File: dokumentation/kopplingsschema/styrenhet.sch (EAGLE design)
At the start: 1 part, among them IC1 MEGA16-P

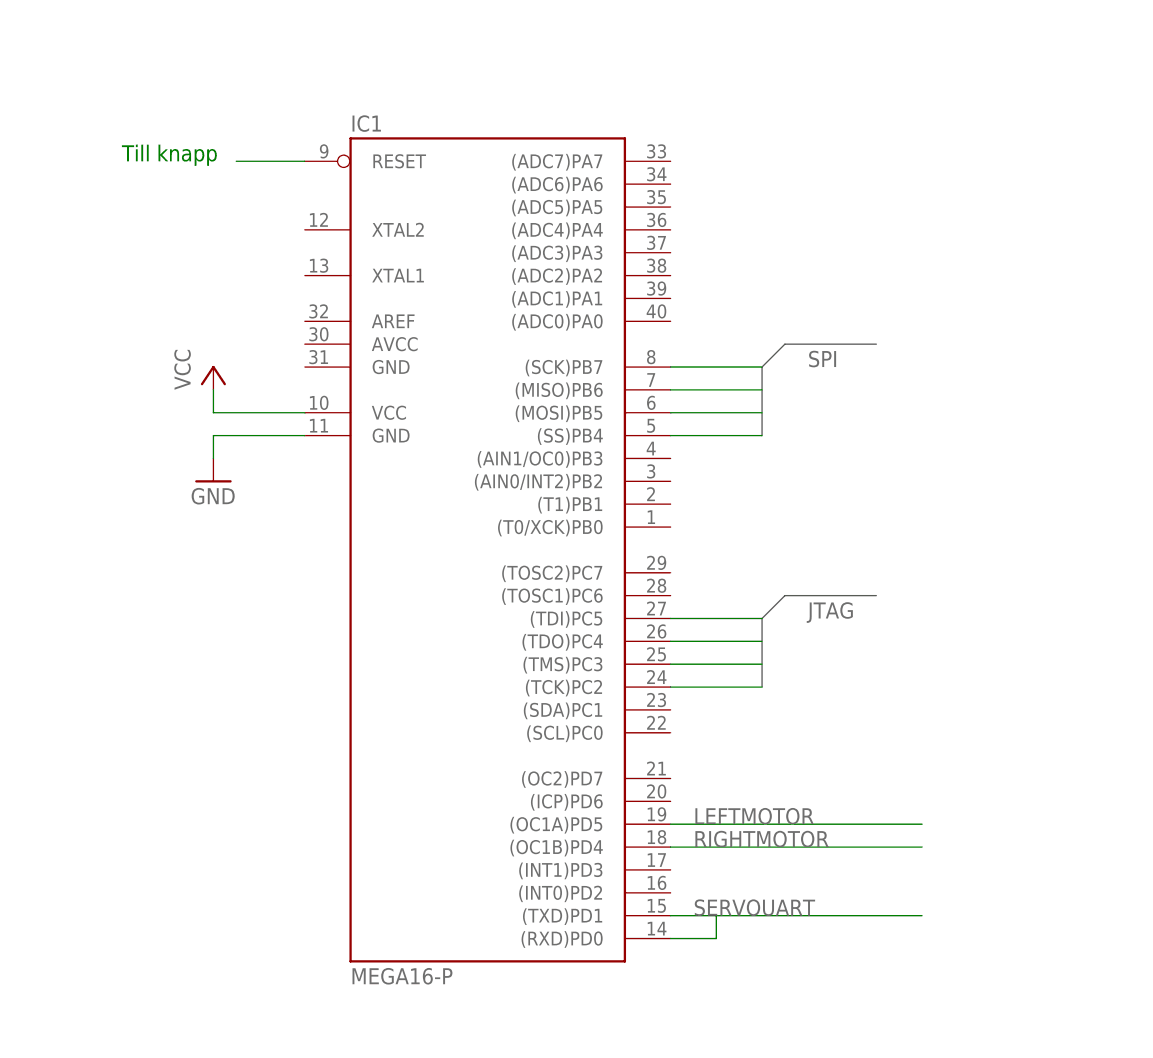
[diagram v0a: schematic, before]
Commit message: Updated circuit diagrams.
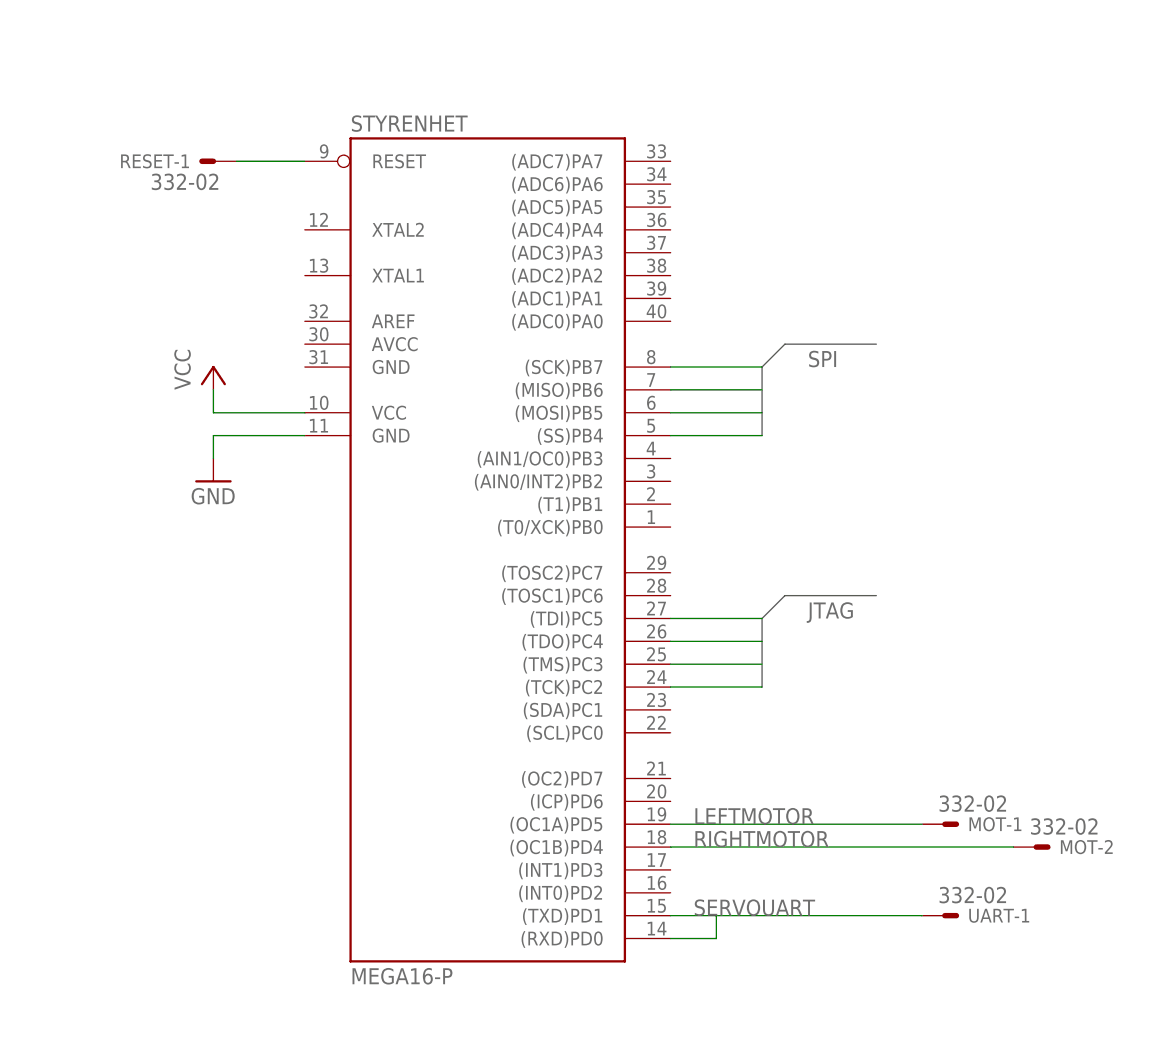
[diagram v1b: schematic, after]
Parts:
- added MOT, RESET, UART: 332-02, con-garry:332-02
- renumbered IC1 to STYRENHET
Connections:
- net LEFTMOTOR: now also MOT-1.S
- net N$1: now also RESET-1.S
- net SERVOUART: now also UART-1.S
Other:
- note removed: "Till knapp"
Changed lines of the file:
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@@
 </classes>
 <parts>
-<part name="IC1" library="atmel" deviceset="MEGA16-P" device=""/>
+<part name="STYRENHET" library="atmel" deviceset="MEGA16-P" device=""/>
 <part name="P+1" library="supply1" deviceset="VCC" device=""/>
 <part name="GND1" library="supply1" deviceset="GND" device=""/>
+<part name="RESET" library="con-garry" deviceset="332-02" device=""/>
+<part name="MOT" library="con-garry" deviceset="332-02" device=""/>
+<part name="UART" library="con-garry" deviceset="332-02" device=""/>
 </parts>
 <sheets>
 <sheet>
 <plain>
-<text x="-25.4" y="88.9" size="1.778" layer="91">Till knapp</text>
 </plain>
 <instances>
-<instance part="IC1" gate="G$1" x="15.24" y="48.26"/>
+<instance part="STYRENHET" gate="G$1" x="15.24" y="48.26"/>
 <instance part="P+1" gate="VCC" x="-15.24" y="66.04"/>
 <instance part="GND1" gate="1" x="-15.24" y="53.34"/>
+<instance part="RESET" gate="-1" x="-15.24" y="88.9" rot="R180"/>
+<instance part="MOT" gate="-1" x="66.04" y="15.24"/>
+<instance part="MOT" gate="-2" x="76.2" y="12.7"/>
+<instance part="UART" gate="-1" x="66.04" y="5.08"/>
 </instances>
 <busses>
@@
 <pinref part="P+1" gate="VCC" pin="VCC"/>
 <wire x1="-15.24" y1="63.5" x2="-15.24" y2="60.96" width="0.1524" layer="91"/>
-<pinref part="IC1" gate="G$1" pin="VCC"/>
+<pinref part="STYRENHET" gate="G$1" pin="VCC"/>
 <wire x1="-15.24" y1="60.96" x2="-5.08" y2="60.96" width="0.1524" layer="91"/>
 </segment>
@@
 <pinref part="GND1" gate="1" pin="GND"/>
 <wire x1="-15.24" y1="55.88" x2="-15.24" y2="58.42" width="0.1524" layer="91"/>
-<pinref part="IC1" gate="G$1" pin="GND"/>
+<pinref part="STYRENHET" gate="G$1" pin="GND"/>
 <wire x1="-15.24" y1="58.42" x2="-5.08" y2="58.42" width="0.1524" layer="91"/>
 </segment>
@@
 <net name="N$1" class="0">
 <segment>
-<pinref part="IC1" gate="G$1" pin="RESET"/>
+<pinref part="STYRENHET" gate="G$1" pin="RESET"/>
 <wire x1="-5.08" y1="88.9" x2="-12.7" y2="88.9" width="0.1524" layer="91"/>
+<pinref part="RESET" gate="-1" pin="S"/>
 </segment>
 </net>
 <net name="N$2" class="0">
 <segment>
-<pinref part="IC1" gate="G$1" pin="(TCK)PC2"/>
+<pinref part="STYRENHET" gate="G$1" pin="(TCK)PC2"/>
 <wire x1="35.56" y1="30.48" x2="45.72" y2="30.48" width="0.1524" layer="91"/>
 </segment>
@@
 <net name="N$3" class="0">
 <segment>
-<pinref part="IC1" gate="G$1" pin="(TMS)PC3"/>
+<pinref part="STYRENHET" gate="G$1" pin="(TMS)PC3"/>
 <wire x1="35.56" y1="33.02" x2="45.72" y2="33.02" width="0.1524" layer="91"/>
 </segment>
@@
 <net name="N$4" class="0">
 <segment>
-<pinref part="IC1" gate="G$1" pin="(TDO)PC4"/>
+<pinref part="STYRENHET" gate="G$1" pin="(TDO)PC4"/>
 <wire x1="35.56" y1="35.56" x2="45.72" y2="35.56" width="0.1524" layer="91"/>
 </segment>
@@
 <net name="N$5" class="0">
 <segment>
-<pinref part="IC1" gate="G$1" pin="(TDI)PC5"/>
+<pinref part="STYRENHET" gate="G$1" pin="(TDI)PC5"/>
 <wire x1="35.56" y1="38.1" x2="45.72" y2="38.1" width="0.1524" layer="91"/>
 </segment>
@@
 <net name="N$6" class="0">
 <segment>
-<pinref part="IC1" gate="G$1" pin="(SS)PB4"/>
+<pinref part="STYRENHET" gate="G$1" pin="(SS)PB4"/>
 <wire x1="35.56" y1="58.42" x2="45.72" y2="58.42" width="0.1524" layer="91"/>
 </segment>
@@
 <net name="N$7" class="0">
 <segment>
-<pinref part="IC1" gate="G$1" pin="(MOSI)PB5"/>
+<pinref part="STYRENHET" gate="G$1" pin="(MOSI)PB5"/>
 <wire x1="35.56" y1="60.96" x2="45.72" y2="60.96" width="0.1524" layer="91"/>
 </segment>
@@
 <net name="N$8" class="0">
 <segment>
-<pinref part="IC1" gate="G$1" pin="(MISO)PB6"/>
+<pinref part="STYRENHET" gate="G$1" pin="(MISO)PB6"/>
 <wire x1="35.56" y1="63.5" x2="45.72" y2="63.5" width="0.1524" layer="91"/>
 </segment>
@@
 <net name="N$9" class="0">
 <segment>
-<pinref part="IC1" gate="G$1" pin="(SCK)PB7"/>
+<pinref part="STYRENHET" gate="G$1" pin="(SCK)PB7"/>
 <wire x1="35.56" y1="66.04" x2="45.72" y2="66.04" width="0.1524" layer="91"/>
 </segment>
@@
 <net name="SERVOUART" class="0">
 <segment>
-<pinref part="IC1" gate="G$1" pin="(TXD)PD1"/>
+<pinref part="STYRENHET" gate="G$1" pin="(TXD)PD1"/>
 <wire x1="35.56" y1="5.08" x2="40.64" y2="5.08" width="0.1524" layer="91"/>
-<pinref part="IC1" gate="G$1" pin="(RXD)PD0"/>
+<pinref part="STYRENHET" gate="G$1" pin="(RXD)PD0"/>
 <wire x1="40.64" y1="5.08" x2="63.5" y2="5.08" width="0.1524" layer="91"/>
 <wire x1="35.56" y1="2.54" x2="40.64" y2="2.54" width="0.1524" layer="91"/>
 <wire x1="40.64" y1="2.54" x2="40.64" y2="5.08" width="0.1524" layer="91"/>
 <label x="38.1" y="5.08" size="1.778" layer="95"/>
+<pinref part="UART" gate="-1" pin="S"/>
 </segment>
 </net>
 <net name="LEFTMOTOR" class="0">
 <segment>
-<pinref part="IC1" gate="G$1" pin="(OC1A)PD5"/>
+<pinref part="STYRENHET" gate="G$1" pin="(OC1A)PD5"/>
 <wire x1="35.56" y1="15.24" x2="63.5" y2="15.24" width="0.1524" layer="91"/>
 <label x="38.1" y="15.24" size="1.778" layer="95"/>
+<pinref part="MOT" gate="-1" pin="S"/>
 </segment>
 </net>
 <net name="RIGHTMOTOR" class="0">
 <segment>
-<pinref part="IC1" gate="G$1" pin="(OC1B)PD4"/>
-<wire x1="35.56" y1="12.7" x2="63.5" y2="12.7" width="0.1524" layer="91"/>
+<pinref part="STYRENHET" gate="G$1" pin="(OC1B)PD4"/>
+<wire x1="35.56" y1="12.7" x2="73.66" y2="12.7" width="0.1524" layer="91"/>
 <label x="38.1" y="12.7" size="1.778" layer="95"/>
 </segment>

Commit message: Updated circuit diagram for prop unit.
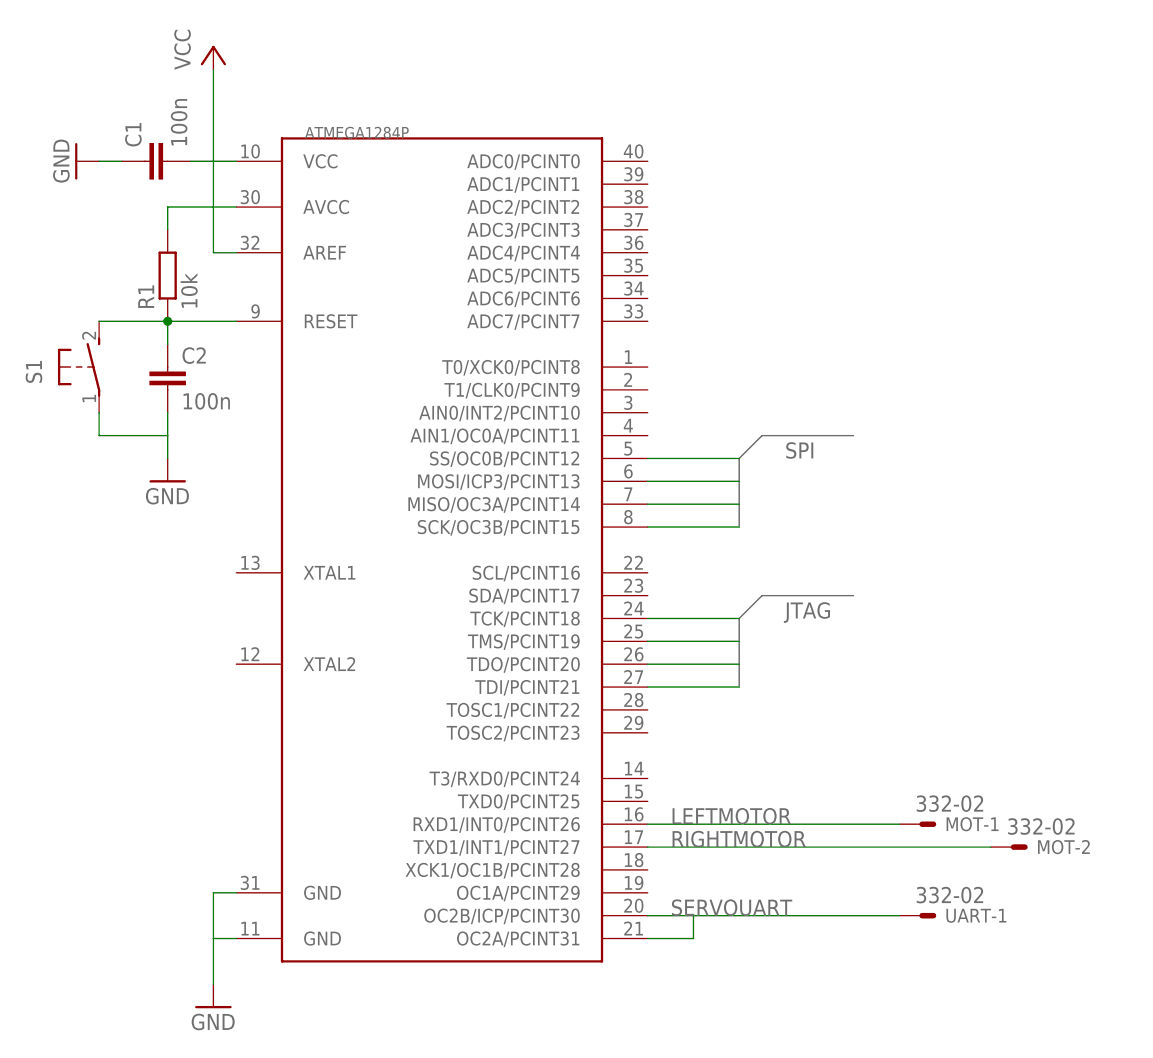
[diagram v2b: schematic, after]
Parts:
- removed RESET: 332-02, con-garry:332-02
- removed STYRENHET: MEGA16-P, atmel:MEGA16-P
- added ATMEGA1284P: (no value), 1284p:MEGA1284P
- added C1, C2: 100n, rcl:C-EU025-050X050
- added R1: 10k, resistor:R-EU_0204/2V
- added S1: (no value), switch-omron:31-XX
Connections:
- removed net N$1: RESET-1.S, STYRENHET.RESET
- removed net N$2: STYRENHET.(TCK)PC2
- removed net N$3: STYRENHET.(TMS)PC3
- removed net N$4: STYRENHET.(TDO)PC4
- removed net N$5: STYRENHET.(TDI)PC5
- removed net N$6: STYRENHET.(SS)PB4
- removed net N$7: STYRENHET.(MOSI)PB5
- removed net N$8: STYRENHET.(MISO)PB6
- removed net N$9: STYRENHET.(SCK)PB7
- new net N$12: ATMEGA1284P.RESET, C2.1, R1.1, S1.S
- net GND: now also ATMEGA1284P.GND@0, ATMEGA1284P.GND@1, C1.1, C2.2, S1.P; no longer STYRENHET.GND
- net LEFTMOTOR: no longer STYRENHET.(OC1A)PD5
- net RIGHTMOTOR: now also MOT-2.S; no longer STYRENHET.(OC1B)PD4
- net SERVOUART: no longer STYRENHET.(RXD)PD0, STYRENHET.(TXD)PD1
- net VCC: now also ATMEGA1284P.AREF, ATMEGA1284P.AVCC, ATMEGA1284P.VCC, C1.2, R1.2; no longer STYRENHET.VCC
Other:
- moved on the sheet: MOT-1, MOT-2, UART-1
